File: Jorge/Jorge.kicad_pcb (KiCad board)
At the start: 2 copper layers, 9 parts

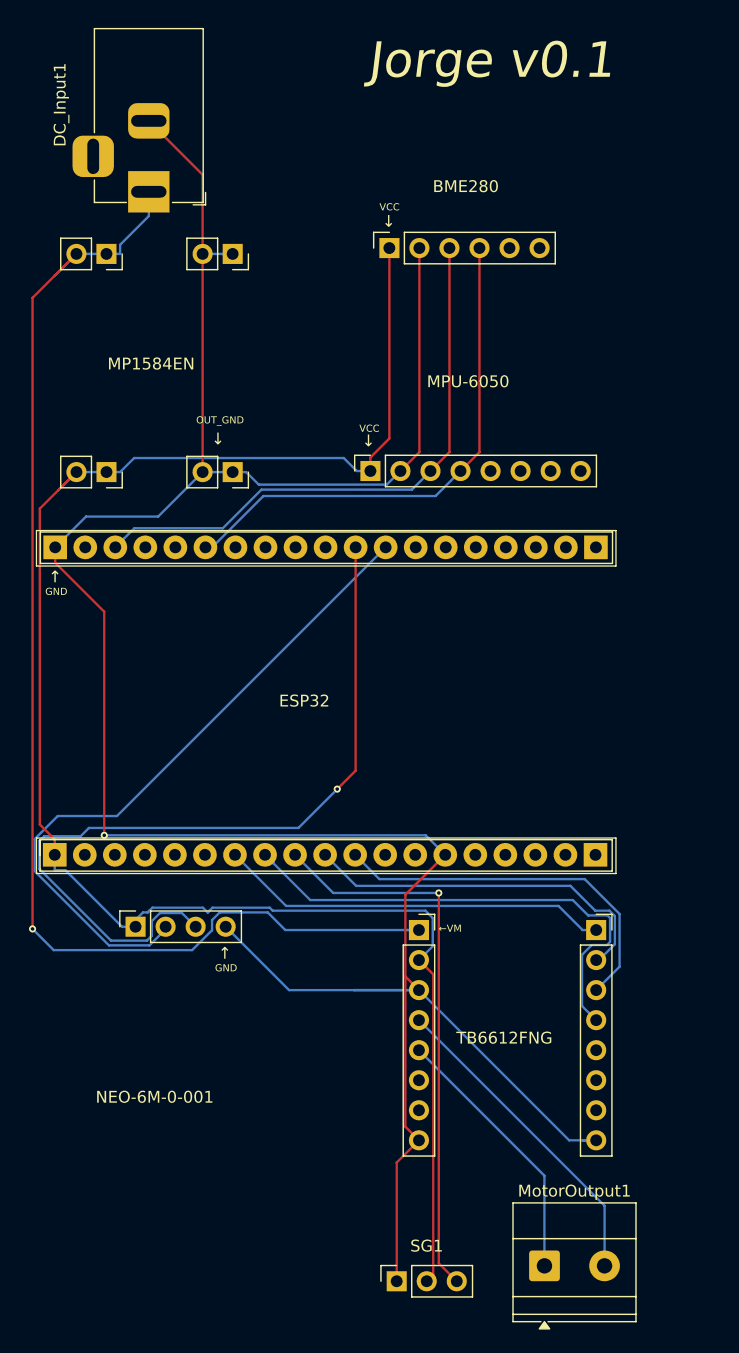
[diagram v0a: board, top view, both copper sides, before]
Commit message: Modified PCB to user Battery 12V -> Regulator 6V -> ESP32 regulator 3.3V system
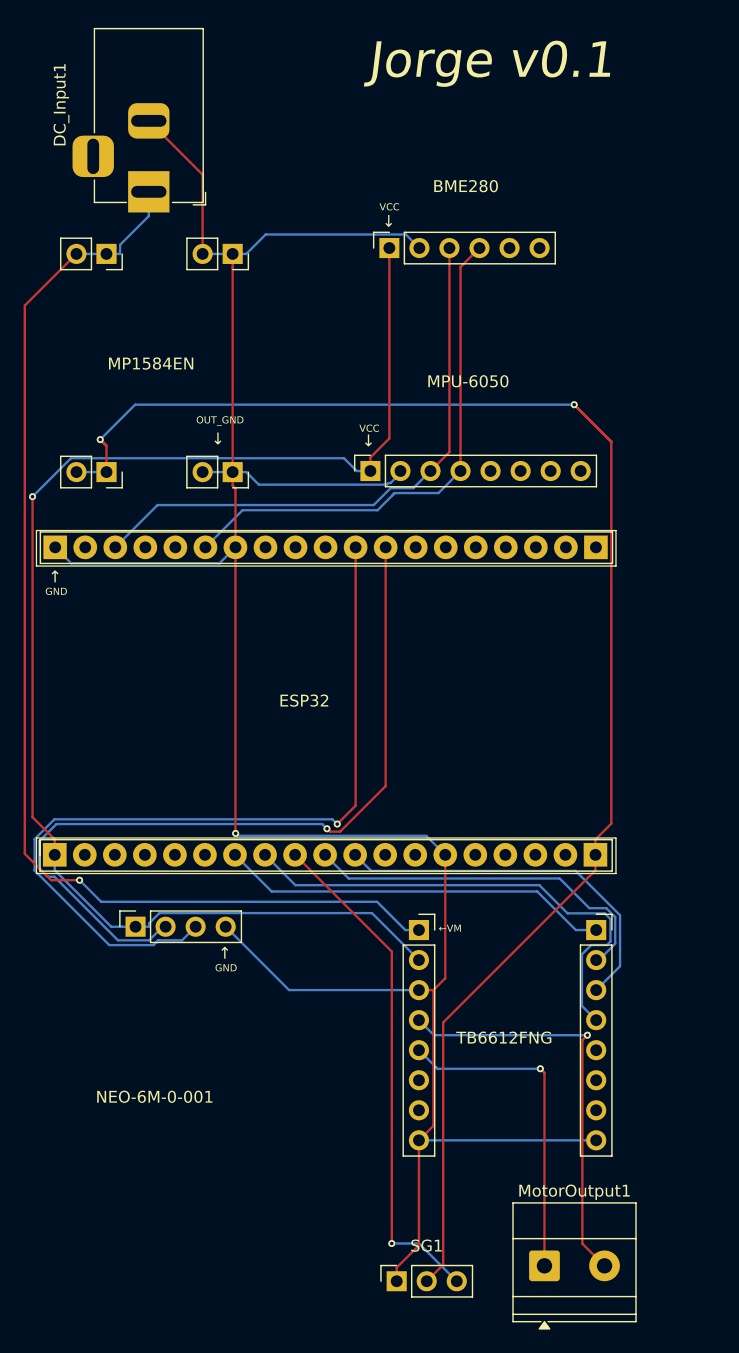
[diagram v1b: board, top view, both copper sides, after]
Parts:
- BMP1: footprint Ernest:BME280_breakout_footprint -> Jorge:BME280_breakout_footprint
- GY-GPS6MV1: footprint Ernest:GY-GPS6MV2_footprint -> Jorge:GY-GPS6MV2_footprint
- MP1584EN1: footprint Ernest:MP1584_breakout_footprint -> Jorge:MP1584_breakout_footprint
- MPU-1: footprint Ernest:MPU6050_breakout_footprint -> Jorge:MPU6050_breakout_footprint
- TB1: footprint Ernest:TB6612_breakout_footprint -> Jorge:TB6612_breakout_footprint
- U1: footprint Esp32DevBoard:ESP32-38pin -> Jorge:ESP32-38pin
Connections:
- MP1584EN1 pad 3: +3.3V -> +6V
- SG1 pad 2: +3.3V -> +6V
- U1 pad 19: unconnected-(U1-5V-Pad19) -> +6V
- U1 pad 32: unconnected-(U1-GND-Pad32) -> GND
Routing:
- net +6V: track 0.00 -> 149.4 mm, vias 0 -> 2
- net +3.3V: track 153.3 -> 117.3 mm, vias 0 -> 1
- net GND: track 230.0 -> 206.8 mm
- net Net-(GY-GPS6MV1-RX): track 57.1 -> 67.9 mm, vias 0 -> 1
- net +12V: track 108.2 -> 98.5 mm
- net Net-(MotorOutput1-Pin_2): track 27.3 -> 35.2 mm, vias 0 -> 1
- net Net-(MotorOutput1-Pin_1): track 22.6 -> 27.7 mm, vias 0 -> 1
- net Net-(SG1-PWM): track 46.9 -> 43.1 mm
- net Net-(GY-GPS6MV1-TX): track 68.3 -> 70.2 mm
- net Net-(TB1-STNDBY): track 44.1 -> 42.3 mm
- net Net-(BMP1-SCL): track 49.9 -> 48.8 mm
